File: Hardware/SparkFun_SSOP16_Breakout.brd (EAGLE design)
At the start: 21.8 x 20.8 mm, 11 parts, among them U1 SSOP16, U2 SSOP16

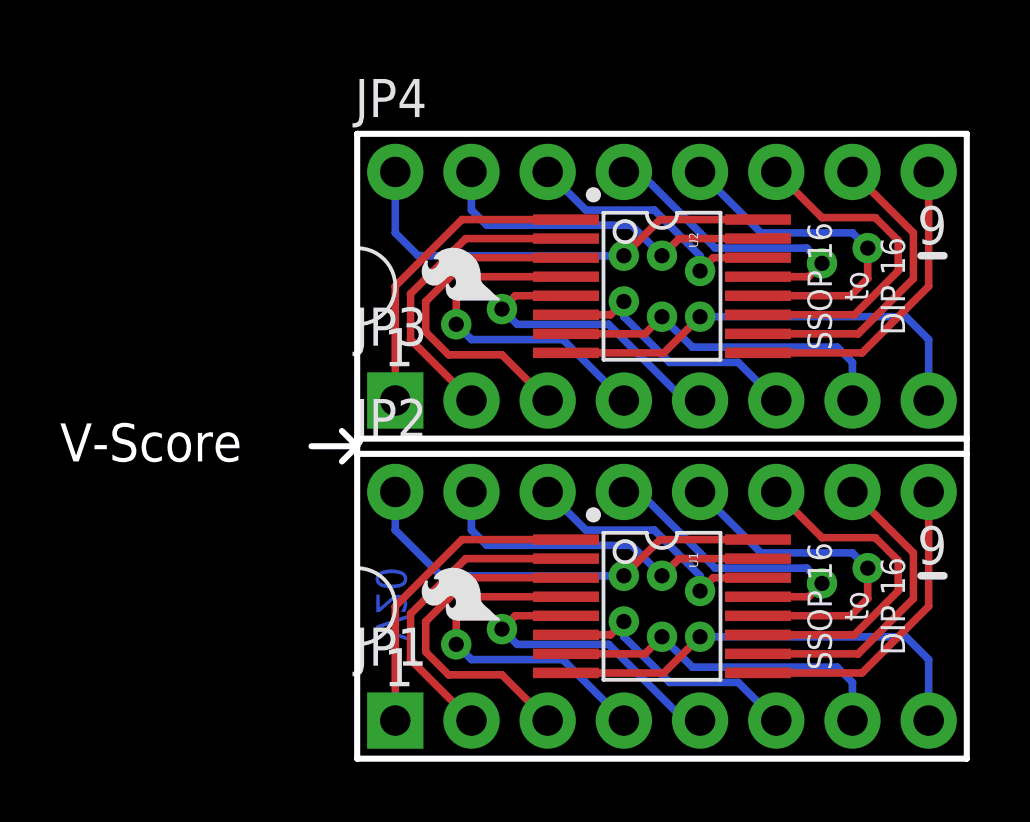
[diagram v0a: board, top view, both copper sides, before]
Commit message: Checklist updates.
Package outline to 8 mil.
Version to V21.
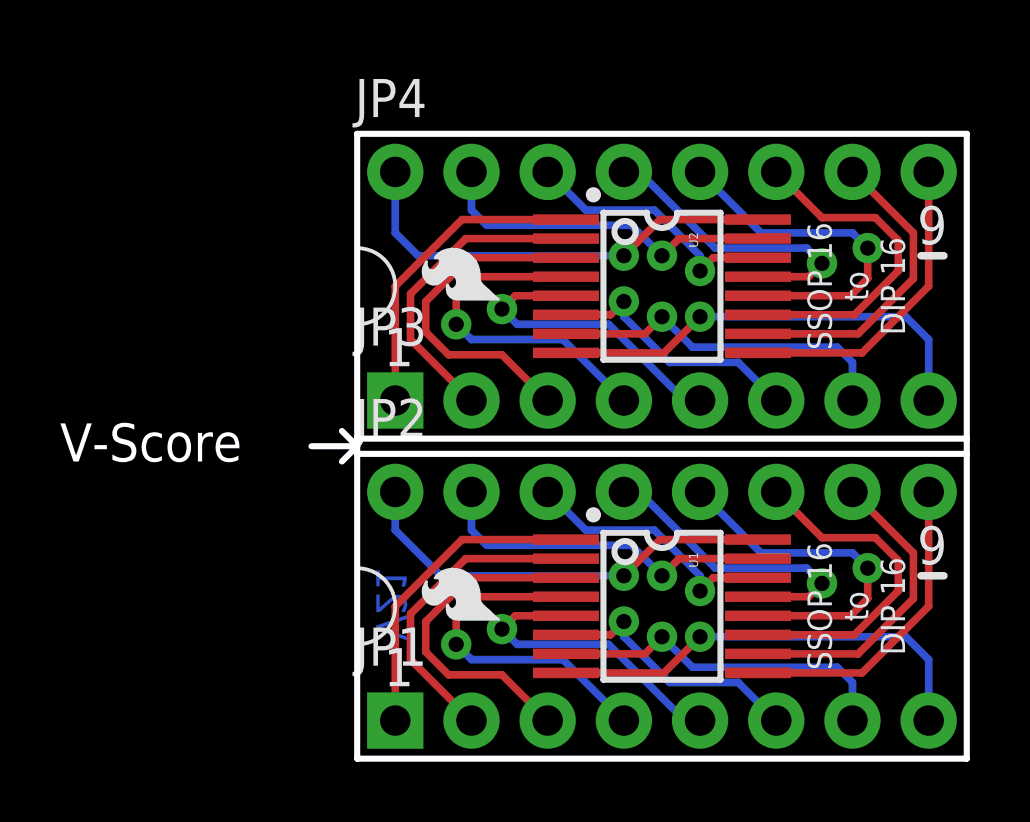
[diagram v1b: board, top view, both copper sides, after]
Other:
- board text added: "V21"
- board text removed: "V20"
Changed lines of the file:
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@@
 <layer number="22" name="bPlace" color="14" fill="1" visible="yes" active="yes"/>
 <layer number="23" name="tOrigins" color="15" fill="1" visible="yes" active="yes"/>
-<layer number="24" name="bOrigins" color="15" fill="1" visible="no" active="yes"/>
-<layer number="25" name="tNames" color="7" fill="1" visible="yes" active="yes"/>
+<layer number="24" name="bOrigins" color="15" fill="1" visible="yes" active="yes"/>
+<layer number="25" name="tNames" color="7" fill="1" visible="no" active="yes"/>
 <layer number="26" name="bNames" color="7" fill="1" visible="no" active="yes"/>
 <layer number="27" name="tValues" color="7" fill="1" visible="no" active="yes"/>
@@
 <layer number="37" name="tTest" color="7" fill="1" visible="no" active="yes"/>
 <layer number="38" name="bTest" color="7" fill="1" visible="no" active="yes"/>
-<layer number="39" name="tKeepout" color="4" fill="11" visible="no" active="yes"/>
-<layer number="40" name="bKeepout" color="1" fill="11" visible="no" active="yes"/>
+<layer number="39" name="tKeepout" color="4" fill="11" visible="yes" active="yes"/>
+<layer number="40" name="bKeepout" color="1" fill="11" visible="yes" active="yes"/>
 <layer number="41" name="tRestrict" color="4" fill="10" visible="no" active="yes"/>
 <layer number="42" name="bRestrict" color="1" fill="10" visible="no" active="yes"/>
 <layer number="43" name="vRestrict" color="2" fill="10" visible="no" active="yes"/>
 <layer number="44" name="Drills" color="7" fill="1" visible="no" active="yes"/>
-<layer number="45" name="Holes" color="7" fill="1" visible="no" active="yes"/>
+<layer number="45" name="Holes" color="7" fill="1" visible="yes" active="yes"/>
 <layer number="46" name="Milling" color="3" fill="1" visible="no" active="yes"/>
-<layer number="47" name="Measures" color="7" fill="1" visible="no" active="yes"/>
+<layer number="47" name="Measures" color="7" fill="1" visible="yes" active="yes"/>
 <layer number="48" name="Document" color="7" fill="1" visible="no" active="yes"/>
 <layer number="49" name="Reference" color="7" fill="1" visible="no" active="yes"/>
 <layer number="50" name="dxf" color="7" fill="1" visible="no" active="yes"/>
-<layer number="51" name="tDocu" color="6" fill="1" visible="no" active="yes"/>
+<layer number="51" name="tDocu" color="6" fill="1" visible="yes" active="yes"/>
 <layer number="52" name="bDocu" color="7" fill="1" visible="no" active="yes"/>
 <layer number="53" name="tGND_GNDA" color="7" fill="9" visible="no" active="no"/>
@@
 <text x="18.669" y="17.145" size="1.27" layer="21" font="vector" ratio="15">9</text>
 <text x="19.431" y="17.145" size="1.27" layer="22" font="vector" ratio="15" rot="MR0">9</text>
-<text x="0.635" y="3.937" size="1.016" layer="16" font="vector" ratio="25" rot="MR90">V20</text>
+<text x="0.635" y="3.937" size="1.016" layer="16" font="vector" ratio="25" rot="MR90">V21</text>
 <wire x1="0" y1="14.478" x2="0" y2="17.018" width="0.127" layer="22" curve="180"/>
 <wire x1="0" y1="17.018" x2="0" y2="14.478" width="0.127" layer="21" curve="-180"/>
